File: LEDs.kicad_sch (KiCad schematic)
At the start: 9 parts, among them Q3 RUM001L02T2CL, Q4 RE1C001ZPTL

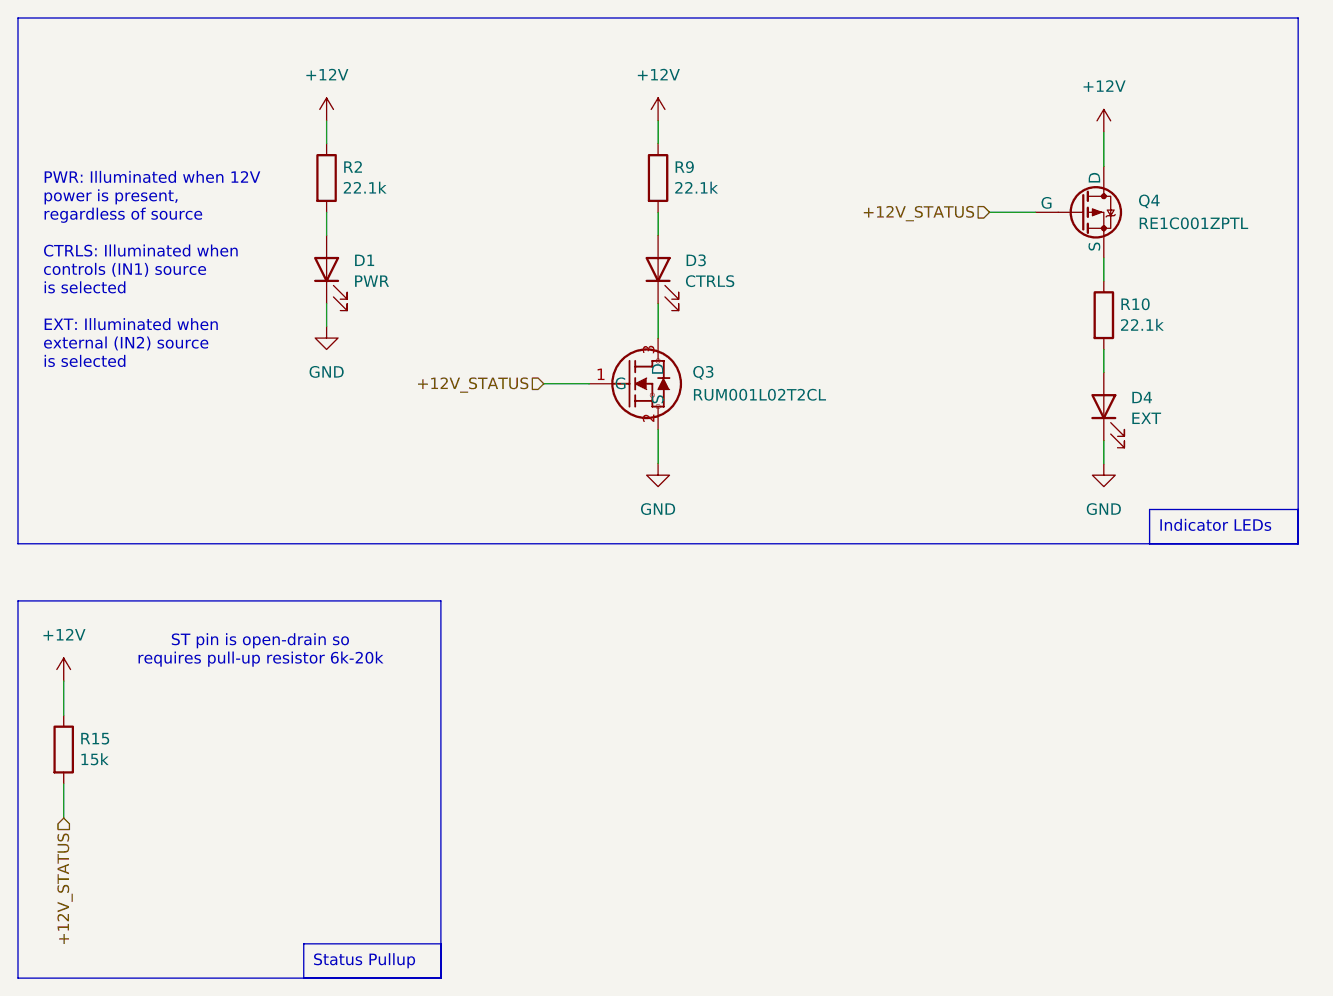
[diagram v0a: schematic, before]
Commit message: modify for PEAK candapter
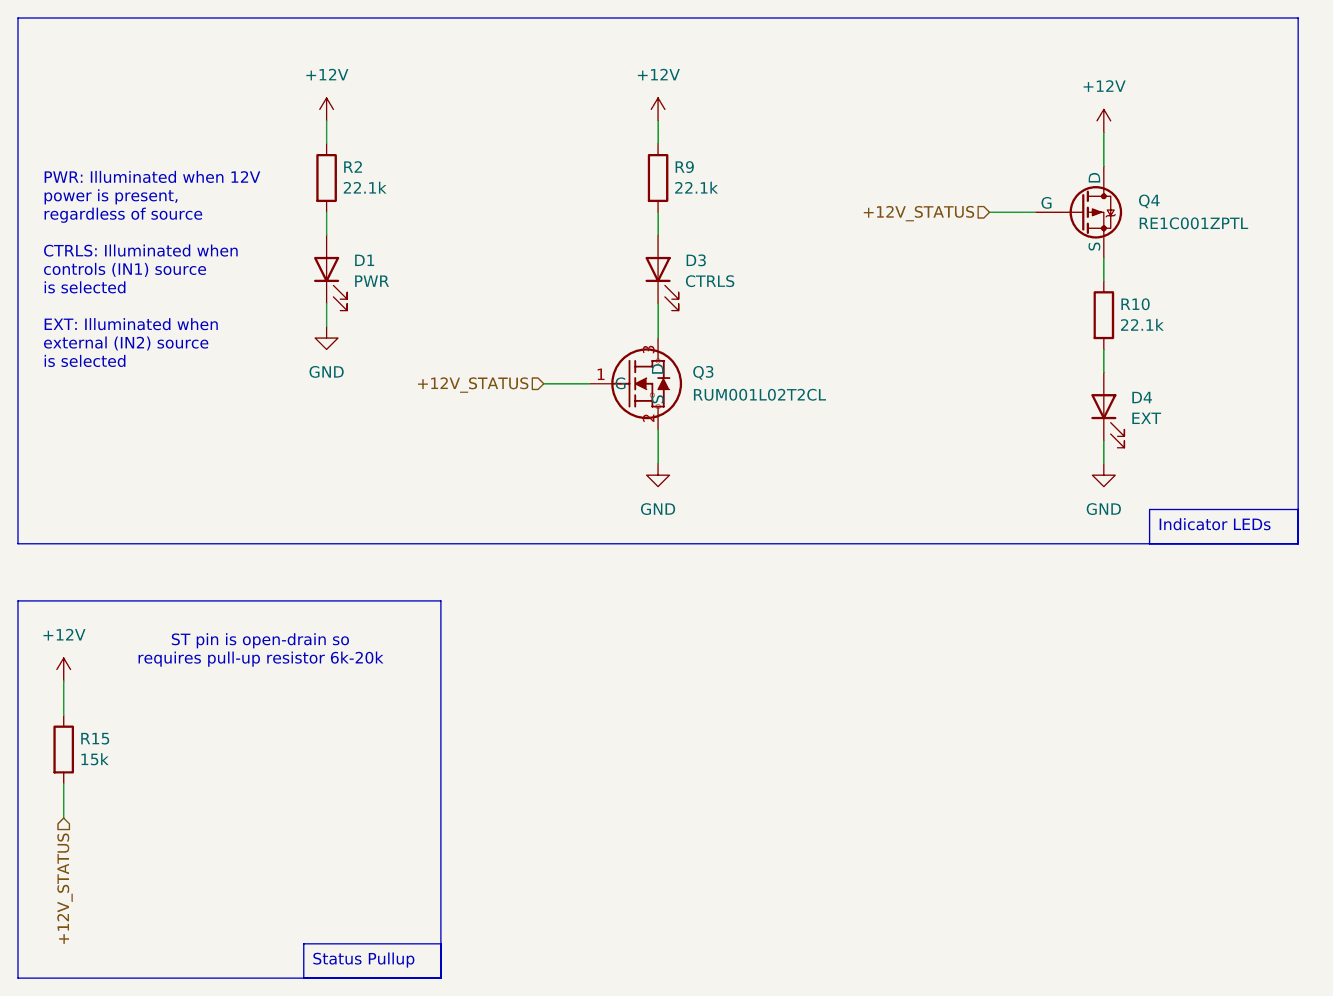
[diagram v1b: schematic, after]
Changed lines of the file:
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@@
 (kicad_sch
-	(version 20231120)
+	(version 20250114)
 	(generator "eeschema")
-	(generator_version "8.0")
+	(generator_version "9.0")
 	(paper "A5")
-	(wire
-		(pts
-			(xy 139.7 31.75) (xy 139.7 35.56)
-		)
-		(stroke
-			(width 0)
-			(type default)
-		)
-	)
-	(wire
-		(pts
-			(xy 139.7 66.04) (xy 139.7 68.58)
-		)
-		(stroke
-			(width 0)
-			(type default)
-		)
-	)
-	(wire
-		(pts
-			(xy 90.17 64.77) (xy 90.17 68.58)
-		)
-		(stroke
-			(width 0)
-			(type default)
-		)
-	)
-	(wire
-		(pts
-			(xy 53.34 40.64) (xy 53.34 43.18)
-		)
-		(stroke
-			(width 0)
-			(type default)
-		)
-	)
-	(wire
-		(pts
-			(xy 90.17 30.48) (xy 90.17 33.02)
-		)
-		(stroke
-			(width 0)
-			(type default)
-		)
-	)
-	(wire
-		(pts
-			(xy 90.17 50.8) (xy 90.17 54.61)
-		)
-		(stroke
-			(width 0)
-			(type default)
-		)
-	)
-	(wire
-		(pts
-			(xy 77.47 59.69) (xy 82.55 59.69)
-		)
-		(stroke
-			(width 0)
-			(type default)
-		)
-	)
-	(wire
-		(pts
-			(xy 53.34 30.48) (xy 53.34 33.02)
-		)
-		(stroke
-			(width 0)
-			(type default)
-		)
-	)
-	(wire
-		(pts
-			(xy 139.7 45.72) (xy 139.7 48.26)
-		)
-		(stroke
-			(width 0)
-			(type default)
-		)
-	)
-	(wire
-		(pts
-			(xy 53.34 50.8) (xy 53.34 53.34)
-		)
-		(stroke
-			(width 0)
-			(type default)
-		)
-	)
-	(wire
-		(pts
-			(xy 90.17 40.64) (xy 90.17 43.18)
-		)
-		(stroke
-			(width 0)
-			(type default)
-		)
-	)
-	(wire
-		(pts
-			(xy 127 40.64) (xy 132.08 40.64)
-		)
-		(stroke
-			(width 0)
-			(type default)
-		)
-	)
-	(wire
-		(pts
-			(xy 139.7 55.88) (xy 139.7 58.42)
-		)
-		(stroke
-			(width 0)
-			(type default)
-		)
-	)
-	(wire
-		(pts
-			(xy 24.13 104.14) (xy 24.13 107.95)
-		)
-		(stroke
-			(width 0)
-			(type default)
-		)
-	)
-	(wire
-		(pts
-			(xy 24.13 92.71) (xy 24.13 96.52)
-		)
-		(stroke
-			(width 0)
-			(type default)
-		)
-	)
 	(rectangle
 		(start 19.05 19.05)
@@
 		)
 	)
+	(text "ST pin is open-drain so\nrequires pull-up resistor 6k-20k"
+		(exclude_from_sim no)
+		(at 45.974 89.408 0)
+		(effects
+			(font
+				(size 1.27 1.27)
+			)
+		)
+	)
+	(text "PWR: Illuminated when 12V\npower is present,\nregardless of source\n\nCTRLS: Illuminated when\ncontrols (IN1) source\nis selected\n\nEXT: Illuminated when\nexternal (IN2) source\nis selected"
+		(exclude_from_sim no)
+		(at 21.844 47.244 0)
+		(effects
+			(font
+				(size 1.27 1.27)
+			)
+			(justify left)
+		)
+	)
 	(text_box "Indicator LEDs"
 		(exclude_from_sim no)
 		(at 144.78 73.66 0)
 		(size 16.51 3.81)
+		(margins 0.9525 0.9525 0.9525 0.9525)
 		(stroke
 			(width 0)
@@
 		(at 50.8 121.92 0)
 		(size 15.24 3.81)
+		(margins 0.9525 0.9525 0.9525 0.9525)
 		(stroke
 			(width 0)
@@
 		)
 	)
-	(text "ST pin is open-drain so\nrequires pull-up resistor 6k-20k"
-		(exclude_from_sim no)
-		(at 45.974 89.408 0)
-		(effects
-			(font
-				(size 1.27 1.27)
-			)
-		)
-	)
-	(text "PWR: Illuminated when 12V\npower is present,\nregardless of source\n\nCTRLS: Illuminated when\ncontrols (IN1) source\nis selected\n\nEXT: Illuminated when\nexternal (IN2) source\nis selected"
-		(exclude_from_sim no)
-		(at 21.844 47.244 0)
-		(effects
-			(font
-				(size 1.27 1.27)
-			)
-			(justify left)
+	(wire
+		(pts
+			(xy 139.7 31.75) (xy 139.7 35.56)
+		)
+		(stroke
+			(width 0)
+			(type default)
+		)
+	)
+	(wire
+		(pts
+			(xy 139.7 66.04) (xy 139.7 68.58)
+		)
+		(stroke
+			(width 0)
+			(type default)
+		)
+	)
+	(wire
+		(pts
+			(xy 90.17 64.77) (xy 90.17 68.58)
+		)
+		(stroke
+			(width 0)
+			(type default)
+		)
+	)
+	(wire
+		(pts
+			(xy 53.34 40.64) (xy 53.34 43.18)
+		)
+		(stroke
+			(width 0)
+			(type default)
+		)
+	)
+	(wire
+		(pts
+			(xy 90.17 30.48) (xy 90.17 33.02)
+		)
+		(stroke
+			(width 0)
+			(type default)
+		)
+	)
+	(wire
+		(pts
+			(xy 90.17 50.8) (xy 90.17 54.61)
+		)
+		(stroke
+			(width 0)
+			(type default)
+		)
+	)
+	(wire
+		(pts
+			(xy 77.47 59.69) (xy 82.55 59.69)
+		)
+		(stroke
+			(width 0)
+			(type default)
+		)
+	)
+	(wire
+		(pts
+			(xy 53.34 30.48) (xy 53.34 33.02)
+		)
+		(stroke
+			(width 0)
+			(type default)
+		)
+	)
+	(wire
+		(pts
+			(xy 139.7 45.72) (xy 139.7 48.26)
+		)
+		(stroke
+			(width 0)
+			(type default)
+		)
+	)
+	(wire
+		(pts
+			(xy 53.34 50.8) (xy 53.34 53.34)
+		)
+		(stroke
+			(width 0)
+			(type default)
+		)
+	)
+	(wire
+		(pts
+			(xy 90.17 40.64) (xy 90.17 43.18)
+		)
+		(stroke
+			(width 0)
+			(type default)
+		)
+	)
+	(wire
+		(pts
+			(xy 127 40.64) (xy 132.08 40.64)
+		)
+		(stroke
+			(width 0)
+			(type default)
+		)
+	)
+	(wire
+		(pts
+			(xy 139.7 55.88) (xy 139.7 58.42)
+		)
+		(stroke
+			(width 0)
+			(type default)
+		)
+	)
+	(wire
+		(pts
+			(xy 24.13 104.14) (xy 24.13 107.95)
+		)
+		(stroke
+			(width 0)
+			(type default)
+		)
+	)
+	(wire
+		(pts
+			(xy 24.13 92.71) (xy 24.13 96.52)
+		)
+		(stroke
+			(width 0)
+			(type default)
 		)
 	)
@@
 		(shape input)
 		(at 127 40.64 180)
-		(fields_autoplaced yes)
 		(effects
 			(font
@@
 		(shape input)
 		(at 24.13 107.95 270)
-		(fields_autoplaced yes)
 		(effects
 			(font
@@
 		(shape input)
 		(at 77.47 59.69 180)
-		(fields_autoplaced yes)
-		(effects
-			(font
+		(effects
+			(font
